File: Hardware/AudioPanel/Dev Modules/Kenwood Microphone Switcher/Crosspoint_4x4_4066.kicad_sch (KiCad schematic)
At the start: 53 parts, among them U201 4066, U202 4066, U203 4066, U204 4066, U205 74HC14, U206 74HC14, U207 74HC14

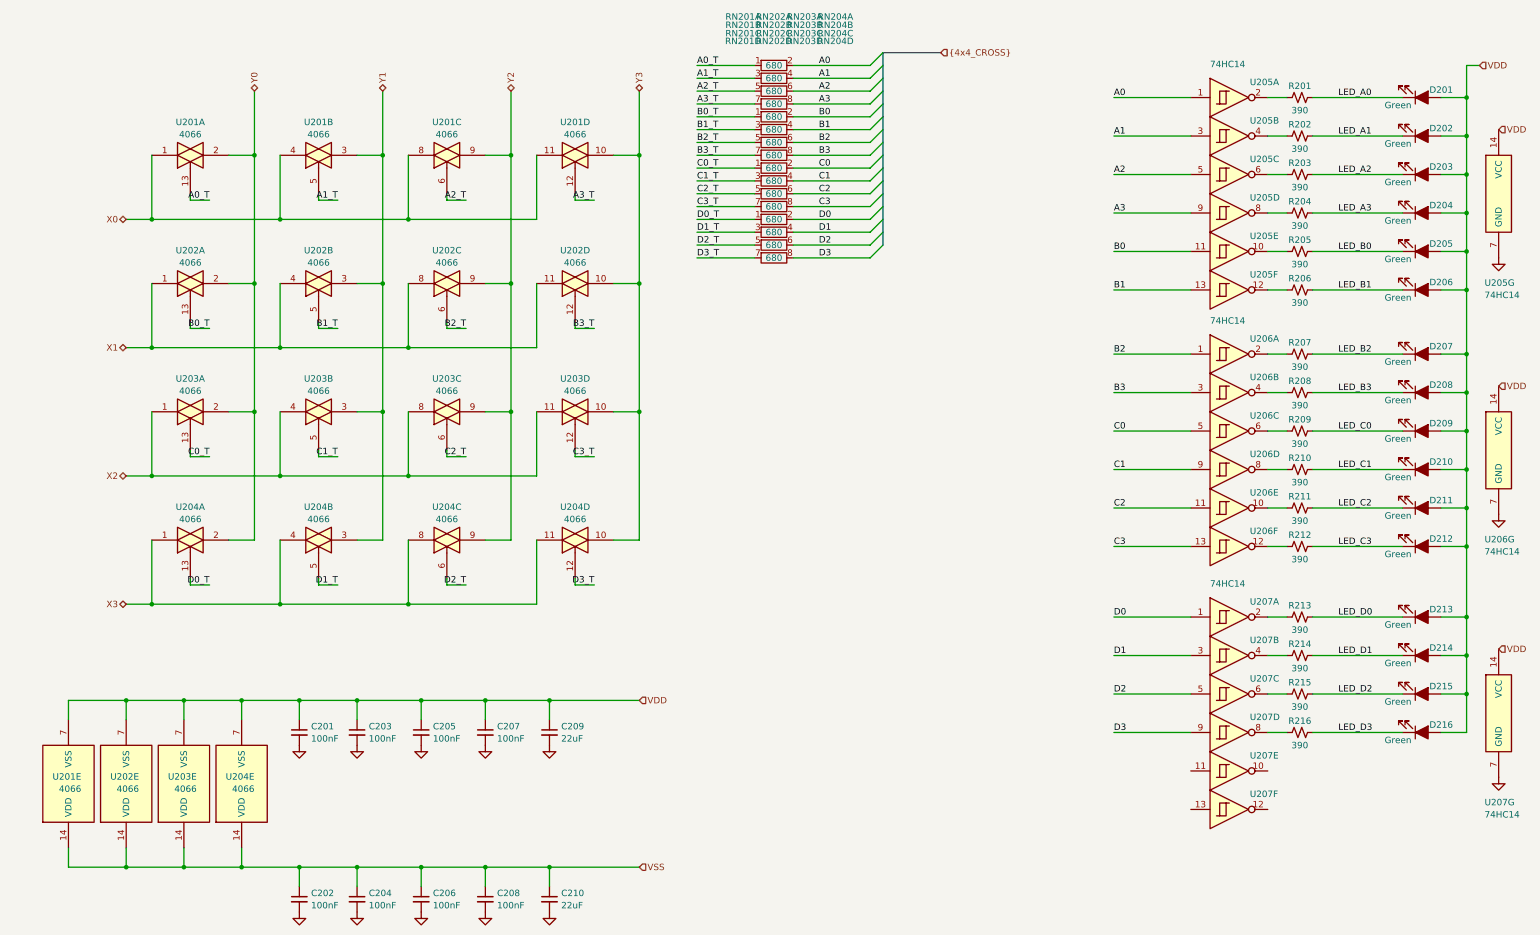
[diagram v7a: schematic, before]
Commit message: Finished most of microphone switcher circuit
I'm very happy with where this is right now, I don't see anything immediately out of place and the schematic is now pretty well organized
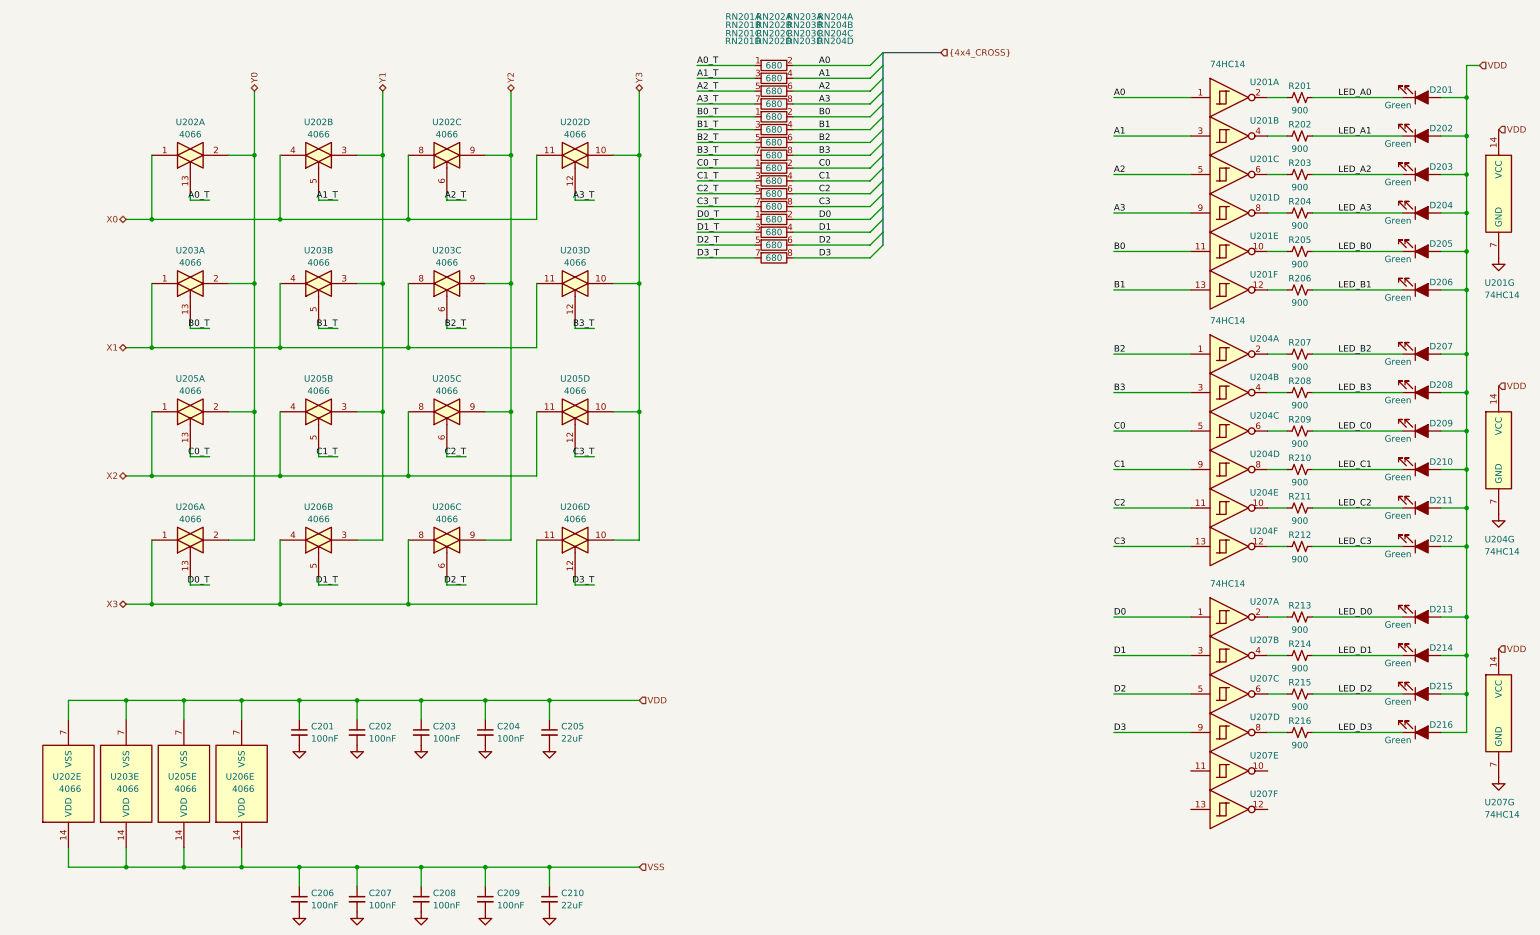
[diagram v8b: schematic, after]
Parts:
- R201, R202, R203, R204, R205, R206, R207, R208, R209, R210, R211, R212, R213, R214, R215, R216: value 390 -> 900
- renumbered C203 to C202, C205 to C203, C207 to C204, C209 to C205, C202 to C206, C204 to C207, C206 to C208, C208 to C209, U205 to U201, U201 to U202, U202 to U203, U206 to U204, U203 to U205, U204 to U206
